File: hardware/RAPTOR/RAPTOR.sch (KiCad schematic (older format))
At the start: 47 parts, among them J1 SOLC_CONN, J10 EXT_LED3, J11 SRVOL_CONN, J12 SRVOR_CONN, J13 HOTWIRE_CONN, J14 RBF_CONN, J15 EEPROM_BTN_CONN, J16 SOLC_SW_CONN, J17 SOLP_SW_CONN, J2 SOLP_CONN, J3 JST_2MM_MALE, J4 CONN_LED_FIX, J5 CONN_SOLP_LED, J6 CONN_SOLC_LED, J7 EXT_LED0, J8 EXT_LED1, J9 EXT_LED2, P1 Power, P2 Analog, P3 Digital, P4 Digital, P5 CONN_01X01, P6 CONN_01X01, P7 CONN_01X01, P8 CONN_01X01, Q1 MOSFET-NCH-2N7002PW, Q2 MOSFET-NCH-2N7002PW, Q3 MOSFET-NCH-2N7002PW, Q4 MOSFET-NCH-2N7002PW, Q5 MOSFET-NCH-2N7002PW, U1 BMP280 Breakout, U2 BNO055 Breakout, U3 OpenLog, U4 AdafruitGPS, U5 U3V12F12, U6 D24V550F5

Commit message: put stuff on pcb thing
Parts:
- Q1, Q2, Q3, Q4, Q5: footprint Silicon-Standard:SOT323 -> Silicon-Standard:TO-92
- R1, R2, R3, R4, R5, R6, R7, R8: footprint 0603 -> Resistor_THT:R_Axial_DIN0204_L3.6mm_D1.6mm_P5.08mm_Horizontal
- U6: footprint (none) -> RAPTOR_footprints:D24v50f5_Reg
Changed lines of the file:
@@
 F 0 "Q1" H 5015 2895 45  0000 L CNN
 F 1 "MOSFET-NCH-2N7002PW" H 5015 2811 45  0000 L CNN
-F 2 "Silicon-Standard:SOT323" H 4850 3100 20  0001 C CNN
+F 2 "Silicon-Standard:TO-92" H 4850 3100 20  0001 C CNN
 F 3 "https://www.diodes.com/assets/Datasheets/ds11303.pdf" H 4850 2800 50  0001 C CNN
 F 4 "TRANS-11151" H 5015 2716 60  0000 L CNN "Field4"
@@
 F 0 "Q3" H 3565 5845 45  0000 L CNN
 F 1 "MOSFET-NCH-2N7002PW" H 3565 5761 45  0000 L CNN
-F 2 "Silicon-Standard:SOT323" H 3400 6050 20  0001 C CNN
+F 2 "Silicon-Standard:TO-92" H 3400 6050 20  0001 C CNN
 F 3 "https://www.diodes.com/assets/Datasheets/ds11303.pdf" H 3400 5750 50  0001 C CNN
 F 4 "TRANS-11151" H 3565 5666 60  0000 L CNN "Field4"
@@
 F 0 "Q4" H 1665 7095 45  0000 L CNN
 F 1 "MOSFET-NCH-2N7002PW" H 1665 7011 45  0000 L CNN
-F 2 "Silicon-Standard:SOT323" H 1500 7300 20  0001 C CNN
+F 2 "Silicon-Standard:TO-92" H 1500 7300 20  0001 C CNN
 F 3 "https://www.diodes.com/assets/Datasheets/ds11303.pdf" H 1500 7000 50  0001 C CNN
 F 4 "TRANS-11151" H 1665 6916 60  0000 L CNN "Field4"
@@
 F 0 "Q2" H 5015 4345 45  0000 L CNN
 F 1 "MOSFET-NCH-2N7002PW" H 5015 4261 45  0000 L CNN
-F 2 "Silicon-Standard:SOT323" H 4850 4550 20  0001 C CNN
+F 2 "Silicon-Standard:TO-92" H 4850 4550 20  0001 C CNN
 F 3 "https://www.diodes.com/assets/Datasheets/ds11303.pdf" H 4850 4250 50  0001 C CNN
 F 4 "TRANS-11151" H 5015 4166 60  0000 L CNN "Field4"
@@
 F 0 "R5" V 8605 4618 45  0000 L CNN
 F 1 "4.7KOHM-0603-1_10W-1%" V 8689 4618 45  0000 L CNN
-F 2 "0603" H 8700 4700 20  0001 C CNN
+F 2 "Resistor_THT:R_Axial_DIN0204_L3.6mm_D1.6mm_P5.08mm_Horizontal" H 8700 4700 20  0001 C CNN
 F 3 "" H 8700 4550 60  0001 C CNN
 F 4 "RES-07857" V 8784 4618 60  0000 L CNN "Field4"
@@
 F 0 "R7" V 9755 4618 45  0000 L CNN
 F 1 "4.7KOHM-0603-1_10W-1%" V 9839 4618 45  0000 L CNN
-F 2 "0603" H 9850 4700 20  0001 C CNN
+F 2 "Resistor_THT:R_Axial_DIN0204_L3.6mm_D1.6mm_P5.08mm_Horizontal" H 9850 4700 20  0001 C CNN
 F 3 "" H 9850 4550 60  0001 C CNN
 F 4 "RES-07857" V 9934 4618 60  0000 L CNN "Field4"
@@
 F 0 "R6" V 9155 6018 45  0000 L CNN
 F 1 "4.7KOHM-0603-1_10W-1%" V 9239 6018 45  0000 L CNN
-F 2 "0603" H 9250 6100 20  0001 C CNN
+F 2 "Resistor_THT:R_Axial_DIN0204_L3.6mm_D1.6mm_P5.08mm_Horizontal" H 9250 6100 20  0001 C CNN
 F 3 "" H 9250 5950 60  0001 C CNN
 F 4 "RES-07857" V 9334 6018 60  0000 L CNN "Field4"
@@
 F 0 "U6" H 3550 1092 50  0000 C CNN
 F 1 "D24V550F5" H 3550 1001 50  0000 C CNN
-F 2 "" H 3575 700 50  0001 L CIN
-F 3 "http://www.st.com/content/ccc/resource/technical/document/datasheet/41/4f/b3/b0/12/d4/47/88/CD00000444.pdf/files/CD00000444.pdf/jcr:content/translations/en.CD00000444.pdf" H 3550 800 50  0001 C CNN
+F 2 "RAPTOR_footprints:D24v50f5_Reg" H 3575 700 50  0001 L CIN
+F 3 "" H 3550 800 50  0001 C CNN
 	1    3550 850
 	1    0    0    -1
@@
 F 0 "R4" H 6000 6950 45  0000 C CNN
 F 1 "100OHM-0603-1_10W-1%" H 6000 6866 45  0000 C CNN
-F 2 "0603" H 6000 6800 20  0001 C CNN
+F 2 "Resistor_THT:R_Axial_DIN0204_L3.6mm_D1.6mm_P5.08mm_Horizontal" H 6000 6800 20  0001 C CNN
 F 3 "" H 6000 6650 60  0001 C CNN
 F 4 "RES-07863" H 6000 6771 60  0000 C CNN "Field4"
@@
 F 0 "R3" H 6000 6250 45  0000 C CNN
 F 1 "100OHM-0603-1_10W-1%" H 6000 6166 45  0000 C CNN
-F 2 "0603" H 6000 6100 20  0001 C CNN
+F 2 "Resistor_THT:R_Axial_DIN0204_L3.6mm_D1.6mm_P5.08mm_Horizontal" H 6000 6100 20  0001 C CNN
 F 3 "" H 6000 5950 60  0001 C CNN
 F 4 "RES-07863" H 6000 6071 60  0000 C CNN "Field4"
@@
 F 0 "R2" H 6000 5500 45  0000 C CNN
 F 1 "100OHM-0603-1_10W-1%" H 6000 5416 45  0000 C CNN
-F 2 "0603" H 6000 5350 20  0001 C CNN
+F 2 "Resistor_THT:R_Axial_DIN0204_L3.6mm_D1.6mm_P5.08mm_Horizontal" H 6000 5350 20  0001 C CNN
 F 3 "" H 6000 5200 60  0001 C CNN
 F 4 "RES-07863" H 6000 5321 60  0000 C CNN "Field4"
@@
 F 0 "R1" V 1505 5768 45  0000 L CNN
 F 1 "20OHM-0603-1_10W-1%" V 1589 5768 45  0000 L CNN
-F 2 "0603" H 1600 5850 20  0001 C CNN
+F 2 "Resistor_THT:R_Axial_DIN0204_L3.6mm_D1.6mm_P5.08mm_Horizontal" H 1600 5850 20  0001 C CNN
 F 3 "" H 1600 5700 60  0001 C CNN
 F 4 "RES-07862" V 1684 5768 60  0000 L CNN "Field4"
@@
 F 0 "Q5" H 7315 3245 45  0000 L CNN
 F 1 "MOSFET-NCH-2N7002PW" H 7315 3161 45  0000 L CNN
-F 2 "Silicon-Standard:SOT323" H 7150 3450 20  0001 C CNN
+F 2 "Silicon-Standard:TO-92" H 7150 3450 20  0001 C CNN
 F 3 "https://www.diodes.com/assets/Datasheets/ds11303.pdf" H 7150 3150 50  0001 C CNN
 F 4 "TRANS-11151" H 7315 3066 60  0000 L CNN "Field4"
@@
 F 0 "R8" V 7155 3668 45  0000 L CNN
 F 1 "4.7KOHM-0603-1_10W-1%" V 7239 3668 45  0000 L CNN
-F 2 "0603" H 7250 3750 20  0001 C CNN
+F 2 "Resistor_THT:R_Axial_DIN0204_L3.6mm_D1.6mm_P5.08mm_Horizontal" H 7250 3750 20  0001 C CNN
 F 3 "" H 7250 3600 60  0001 C CNN
 F 4 "RES-07857" V 7334 3668 60  0000 L CNN "Field4"
@@
 	3600 3200 3950 3200
 $Comp
-L power:GND #PWR?
+L power:GND #PWR08
 U 1 1 5C859293
 P 3550 1300
-F 0 "#PWR?" H 3550 1050 50  0001 C CNN
+F 0 "#PWR08" H 3550 1050 50  0001 C CNN
 F 1 "GND" H 3555 1127 50  0000 C CNN
 F 2 "" H 3550 1300 50  0001 C CNN

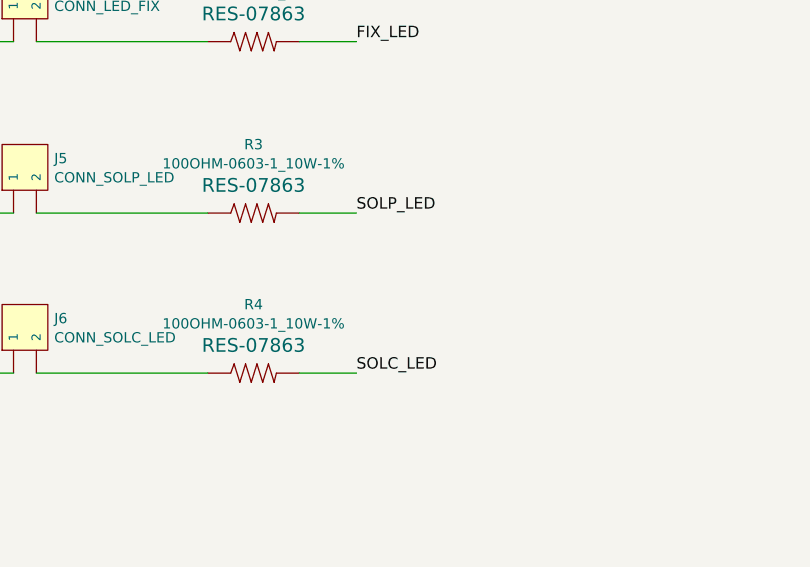
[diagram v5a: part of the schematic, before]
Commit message: Fitted parts
Placed all the compnents on the actual PCB not just off to the side
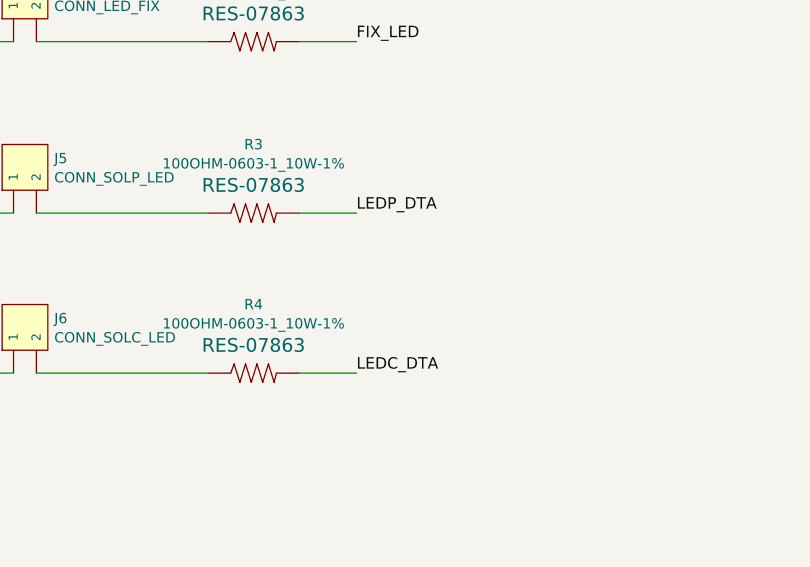
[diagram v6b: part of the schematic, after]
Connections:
- net SOLC_LED is gone; now on net LEDC_DTA: R4.2
- net SOLP_LED is gone; now on net LEDP_DTA: R3.2
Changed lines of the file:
@@
 	4600 5200 4950 5200
 Text Label 6450 5950 0    50   ~ 0
-SOLP_LED
+LEDP_DTA
 $Comp
 L power:GND #PWR019
@@
 	4600 5950 4950 5950
 Text Label 6450 6650 0    50   ~ 0
-SOLC_LED
+LEDC_DTA
 $Comp
 L power:GND #PWR020

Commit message: PCB Error Fixing
Changed footprints and symbols to be more accurate
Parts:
- J3: footprint CONN-BATT -> RAPTOR_footprints:2_Pin_Connector
- P2: footprint Socket_Arduino_Uno:Socket_Strip_Arduino_1x06 -> RAPTOR_footprints:Arduino_Analog_06
- P3: footprint Socket_Arduino_Uno:Socket_Strip_Arduino_1x10 -> RAPTOR_footprints:Arduino_x10_Digital
- P4: footprint Socket_Arduino_Uno:Socket_Strip_Arduino_1x08 -> RAPTOR_footprints:Arduino_x08_Digital
- U6: symbol Regulator_Linear:L7805 -> RAPTOR-rescue:D24V50F5
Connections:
- net Vin is gone; now on net +7.5V: P1.8 (Pin_8)
- net +5V: now also U6.5 (VOUT); no longer U6.3 (OUT)
- net +7.5V: now also U6.2 (VIN); no longer U6.1 (IN)
- net GND: now also U6.3 (GND), U6.4 (GND); no longer U6.2 (GND)
- no-connect marks 19 -> 20
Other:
- moved on the sheet: U5
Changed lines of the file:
@@
 Comment4 "Arduino (HiLetGo UNO R3) Shield"
 $EndDescr
-Text Label 8950 1450 1    60   ~ 0
-Vin
 Text Label 9350 1450 1    60   ~ 0
 IOREF
@@
 F 0 "P2" H 9600 2300 50  0000 C CNN
 F 1 "Analog" V 9700 2700 50  0000 C CNN
-F 2 "Socket_Arduino_Uno:Socket_Strip_Arduino_1x06" V 9750 2750 20  0000 C CNN
+F 2 "RAPTOR_footprints:Arduino_Analog_06" V 9750 2750 20  0000 C CNN
 F 3 "" H 9600 2700 50  0000 C CNN
 	1    9600 2700
@@
 F 0 "P4" H 10000 2100 50  0000 C CNN
 F 1 "Digital" V 10100 2600 50  0000 C CNN
-F 2 "Socket_Arduino_Uno:Socket_Strip_Arduino_1x08" V 10150 2550 20  0000 C CNN
+F 2 "RAPTOR_footprints:Arduino_x08_Digital" V 10150 2550 20  0000 C CNN
 F 3 "" H 10000 2600 50  0000 C CNN
 	1    10000 2600
@@
 F 0 "P3" H 10000 2250 50  0000 C CNN
 F 1 "Digital" V 10100 1700 50  0000 C CNN
-F 2 "Socket_Arduino_Uno:Socket_Strip_Arduino_1x10" V 10150 1700 20  0000 C CNN
+F 2 "RAPTOR_footprints:Arduino_x10_Digital" V 10150 1700 20  0000 C CNN
 F 3 "" H 10000 1700 50  0000 C CNN
 	1    10000 1700
@@
 L power:GND #PWR012
 U 1 1 5C40FAEF
-P 3550 2350
-F 0 "#PWR012" H 3550 2100 50  0001 C CNN
-F 1 "GND" H 3555 2177 50  0000 C CNN
-F 2 "" H 3550 2350 50  0001 C CNN
-F 3 "" H 3550 2350 50  0001 C CNN
-	1    3550 2350
-	1    0    0    -1
-$EndComp
-Wire Wire Line
-	3550 2200 3550 2350
+P 3550 2400
+F 0 "#PWR012" H 3550 2150 50  0001 C CNN
+F 1 "GND" H 3555 2227 50  0000 C CNN
+F 2 "" H 3550 2400 50  0001 C CNN
+F 3 "" H 3550 2400 50  0001 C CNN
+	1    3550 2400
+	1    0    0    -1
+$EndComp
+Wire Wire Line
+	3550 2250 3550 2400
 $Comp
 L power:+7.5V #PWR011
 U 1 1 5C42772B
-P 3000 1850
-F 0 "#PWR011" H 3000 1700 50  0001 C CNN
-F 1 "+7.5V" H 3015 2023 50  0001 C CNN
-F 2 "" H 3000 1850 50  0001 C CNN
-F 3 "" H 3000 1850 50  0001 C CNN
-F 4 "+7.4V" H 3015 2023 50  0000 C CNN "Real Value"
-	1    3000 1850
-	1    0    0    -1
-$EndComp
-Wire Wire Line
-	3250 1900 3000 1900
-Wire Wire Line
-	3850 1900 4100 1900
+P 3000 1900
+F 0 "#PWR011" H 3000 1750 50  0001 C CNN
+F 1 "+7.5V" H 3015 2073 50  0001 C CNN
+F 2 "" H 3000 1900 50  0001 C CNN
+F 3 "" H 3000 1900 50  0001 C CNN
+F 4 "+7.4V" H 3015 2073 50  0000 C CNN "Real Value"
+	1    3000 1900
+	1    0    0    -1
+$EndComp
+Wire Wire Line
+	3250 1950 3000 1950
+Wire Wire Line
+	3850 1950 4100 1950
 $Comp
 L power:+12V #PWR013
 U 1 1 5C4334FC
-P 4100 1850
-F 0 "#PWR013" H 4100 1700 50  0001 C CNN
-F 1 "+12V" H 4115 2115 50  0000 C CNN
-F 2 "" H 4100 1850 50  0001 C CNN
-F 3 "" H 4100 1850 50  0001 C CNN
-F 4 "(TO SOLENOID)" H 4115 2024 50  0000 C CNN "Note"
-	1    4100 1850
+P 4100 1900
+F 0 "#PWR013" H 4100 1750 50  0001 C CNN
+F 1 "+12V" H 4115 2165 50  0000 C CNN
+F 2 "" H 4100 1900 50  0001 C CNN
+F 3 "" H 4100 1900 50  0001 C CNN
+F 4 "(TO SOLENOID)" H 4115 2074 50  0000 C CNN "Note"
+	1    4100 1900
 	1    0    0    -1
 $EndComp
@@
 L power:+7.5V #PWR06
 U 1 1 5C49E027
-P 3000 850
-F 0 "#PWR06" H 3000 700 50  0001 C CNN
-F 1 "+7.5V" H 3015 1023 50  0001 C CNN
-F 2 "" H 3000 850 50  0001 C CNN
-F 3 "" H 3000 850 50  0001 C CNN
-F 4 "+7.4V" H 3015 1023 50  0000 C CNN "Real Value"
-	1    3000 850
+P 4100 900
+F 0 "#PWR06" H 4100 750 50  0001 C CNN
+F 1 "+7.5V" H 4115 1073 50  0001 C CNN
+F 2 "" H 4100 900 50  0001 C CNN
+F 3 "" H 4100 900 50  0001 C CNN
+F 4 "+7.4V" H 4115 1073 50  0000 C CNN "Real Value"
+	1    4100 900
 	1    0    0    -1
 $EndComp
@@
 L power:+5V #PWR010
 U 1 1 5C49E02F
-P 4100 850
-F 0 "#PWR010" H 4100 700 50  0001 C CNN
-F 1 "+5V" H 4115 1023 50  0000 C CNN
-F 2 "" H 4100 850 50  0001 C CNN
-F 3 "" H 4100 850 50  0001 C CNN
-	1    4100 850
-	1    0    0    -1
-$EndComp
-Wire Wire Line
-	3000 1900 3000 1850
-Wire Wire Line
-	4100 1900 4100 1850
+P 3000 1000
+F 0 "#PWR010" H 3000 850 50  0001 C CNN
+F 1 "+5V" H 3015 1173 50  0000 C CNN
+F 2 "" H 3000 1000 50  0001 C CNN
+F 3 "" H 3000 1000 50  0001 C CNN
+	1    3000 1000
+	1    0    0    -1
+$EndComp
+Wire Wire Line
+	3000 1950 3000 1900
+Wire Wire Line
+	4100 1950 4100 1900
 $Comp
 L power:GND #PWR016
@@
 L RAPTOR-rescue:U3V12F12 U5
 U 1 1 5C3DF905
-P 3550 1900
-F 0 "U5" H 3550 2142 50  0000 C CNN
-F 1 "U3V12F12" H 3550 2051 50  0000 C CNN
-F 2 "RAPTOR_footprints:U3V12F12" H 3550 2150 50  0001 C CNN
-F 3 "" H 3550 2150 50  0001 C CNN
-	1    3550 1900
+P 3550 1950
+F 0 "U5" H 3550 2192 50  0000 C CNN
+F 1 "U3V12F12" H 3550 2101 50  0000 C CNN
+F 2 "RAPTOR_footprints:U3V12F12" H 3550 2200 50  0001 C CNN
+F 3 "" H 3550 2200 50  0001 C CNN
+	1    3550 1950
 	1    0    0    -1
 $EndComp
@@
 F 0 "J3" V 3473 3444 45  0000 C CNN
 F 1 "JST_2MM_MALE" H 3150 3250 45  0001 L BNN
-F 2 "CONN-BATT" V 3389 3444 45  0000 C CNN
+F 2 "RAPTOR_footprints:2_Pin_Connector" V 3389 3444 45  0000 C CNN
 F 3 "" H 3050 3450 50  0001 C CNN
 F 4 "CONN-11443" V 3294 3444 60  0000 C CNN "Field4"
@@
 	1300 7100 1150 7100
 $Comp
-L Regulator_Linear:L7805 U6
+L RAPTOR-rescue:D24V50F5 U6
 U 1 1 5C49E003
-P 3550 850
-F 0 "U6" H 3550 1092 50  0000 C CNN
-F 1 "D24V550F5" H 3550 1001 50  0000 C CNN
-F 2 "RAPTOR_footprints:D24v50f5_Reg" H 3575 700 50  0001 L CIN
-F 3 "" H 3550 800 50  0001 C CNN
-	1    3550 850
+P 3550 800
+F 0 "U6" H 3550 1042 50  0000 C CNN
+F 1 "D24V550F5" H 3550 951 50  0000 C CNN
+F 2 "RAPTOR_footprints:D24v50f5_Reg" H 3575 650 50  0001 L CIN
+F 3 "" H 3550 750 50  0001 C CNN
+	1    3550 800
 	1    0    0    -1
 $EndComp
@@
 Wire Wire Line
 	3600 3200 3950 3200
-$Comp
-L power:GND #PWR08
-U 1 1 5C859293
-P 3550 1300
-F 0 "#PWR08" H 3550 1050 50  0001 C CNN
-F 1 "GND" H 3555 1127 50  0000 C CNN
-F 2 "" H 3550 1300 50  0001 C CNN
-F 3 "" H 3550 1300 50  0001 C CNN
-	1    3550 1300
-	1    0    0    -1
-$EndComp
-Wire Wire Line
-	3550 1150 3550 1300
-Wire Wire Line
-	3000 850  3250 850
-Wire Wire Line
-	4100 850  3850 850
+Wire Wire Line
+	4100 900  3850 900
+Wire Wire Line
+	3000 1000 3250 1000
+$Comp
+L power:+7.5V #PWR0109
+U 1 1 5C458694
+P 8950 1450
+F 0 "#PWR0109" H 8950 1300 50  0001 C CNN
+F 1 "+7.5V" H 8965 1623 50  0001 C CNN
+F 2 "" H 8950 1450 50  0001 C CNN
+F 3 "" H 8950 1450 50  0001 C CNN
+F 4 "+7.4V" H 8965 1623 50  0000 C CNN "Real Value"
+	1    8950 1450
+	1    0    0    -1
+$EndComp
+Wire Wire Line
+	3450 1300 3450 1400
+Wire Wire Line
+	3450 1400 3550 1400
+Wire Wire Line
+	3650 1400 3650 1300
+$Comp
+L power:GND #PWR0111
+U 1 1 5C512703
+P 3550 1400
+F 0 "#PWR0111" H 3550 1150 50  0001 C CNN
+F 1 "GND" H 3555 1227 50  0000 C CNN
+F 2 "" H 3550 1400 50  0001 C CNN
+F 3 "" H 3550 1400 50  0001 C CNN
+	1    3550 1400
+	1    0    0    -1
+$EndComp
+Connection ~ 3550 1400
+Wire Wire Line
+	3550 1400 3650 1400
+NoConn ~ 3250 900
 $EndSCHEMATC

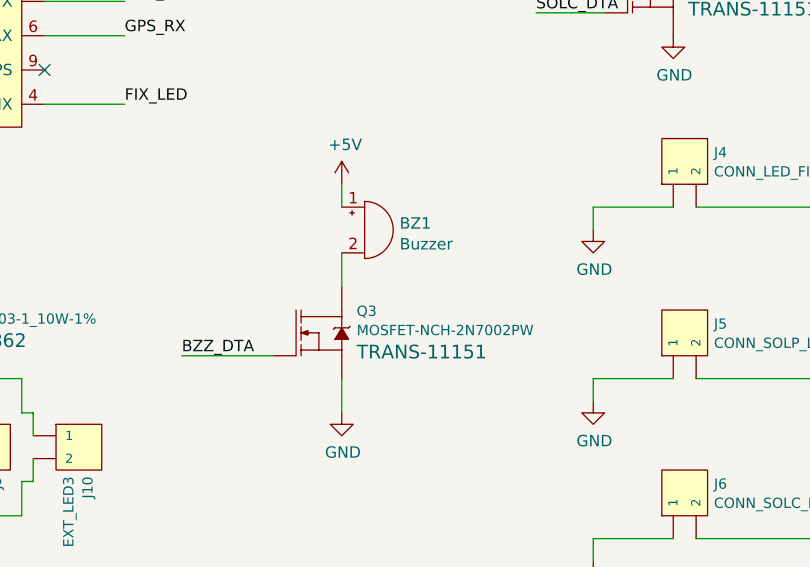
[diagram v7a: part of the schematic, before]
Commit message: add connector for buzzer, resolves #72
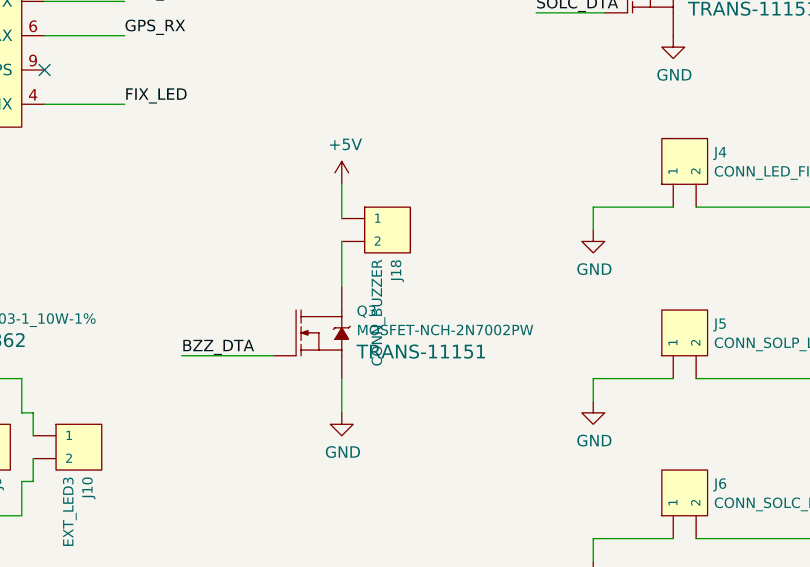
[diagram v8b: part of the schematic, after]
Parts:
- removed BZ1: Buzzer, Buzzer_Beeper:Buzzer_12x9.5RM7.6, symbol Device:Buzzer
- added J18: CONN_BUZZER, Connectors:1X02, symbol RAPTOR-rescue:CONN_02-SparkFun-Connectors
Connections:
- net +5V: now also J18.1
- net at Q3.3 (D): now also J18.2
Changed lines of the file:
@@
 	4950 2100 4950 2200
-$Comp
-L Device:Buzzer BZ1
-U 1 1 5BEADE3C
-P 3600 5300
-F 0 "BZ1" H 3753 5329 50  0000 L CNN
-F 1 "Buzzer" H 3753 5238 50  0000 L CNN
-F 2 "Buzzer_Beeper:Buzzer_12x9.5RM7.6" V 3575 5400 50  0001 C CNN
-F 3 "~" V 3575 5400 50  0001 C CNN
-	1    3600 5300
-	1    0    0    -1
-$EndComp
 $Comp
 L RAPTOR-rescue:MOSFET-NCH-2N7002PW-SparkFun-DiscreteSemi Q3
@@
 Wire Wire Line
 	3200 5850 2800 5850
-Wire Wire Line
-	3500 5400 3500 5550
 $Comp
 L power:GND #PWR0116
@@
 Wire Wire Line
 	3500 5950 3500 6100
-Wire Wire Line
-	3500 5200 3500 5100
 Text Label 6450 5200 0    50   ~ 0
 FIX_LED
@@
 	3550 1400 3650 1400
 NoConn ~ 3250 900
+$Comp
+L RAPTOR-rescue:CONN_02-SparkFun-Connectors J18
+U 1 1 5C4A4245
+P 3600 5250
+F 0 "J18" V 3461 5428 45  0000 L CNN
+F 1 "CONN_BUZZER" V 3545 5428 45  0000 L CNN
+F 2 "Connectors:1X02" H 3600 5500 20  0001 C CNN
+F 3 "" H 3600 5250 50  0001 C CNN
+F 4 "XXX-00000" V 3640 5428 60  0001 L CNN "Field4"
+	1    3600 5250
+	-1   0    0    1
+$EndComp
+Wire Wire Line
+	3500 5100 3500 5250
+Wire Wire Line
+	3500 5350 3500 5550
 $EndSCHEMATC
